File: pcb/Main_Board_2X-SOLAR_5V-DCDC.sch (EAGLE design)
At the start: 67 parts, among them CN5 USBA_FEMALE, M3AB FDMC8030, M4 SI7611DN, M5 FDMC8327L, T2 MMUN2133LT1G, U1 LTC4015EUHFPBFQFN-38_UHF-M, U3 TPS61090RSAR, X1 6V_PV

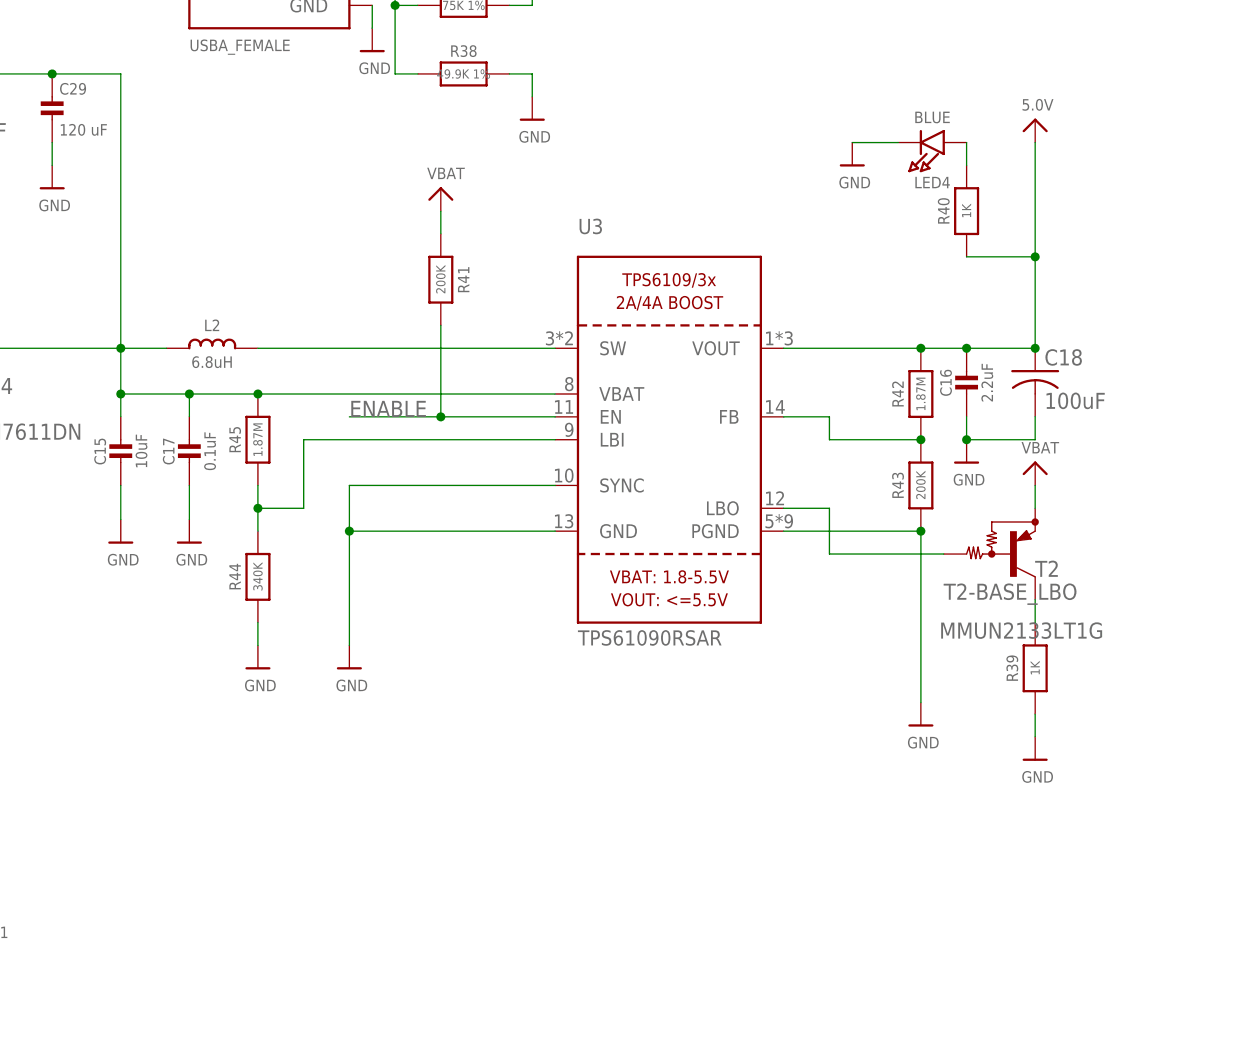
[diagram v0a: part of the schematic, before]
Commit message: PCB ready to print, reviewing
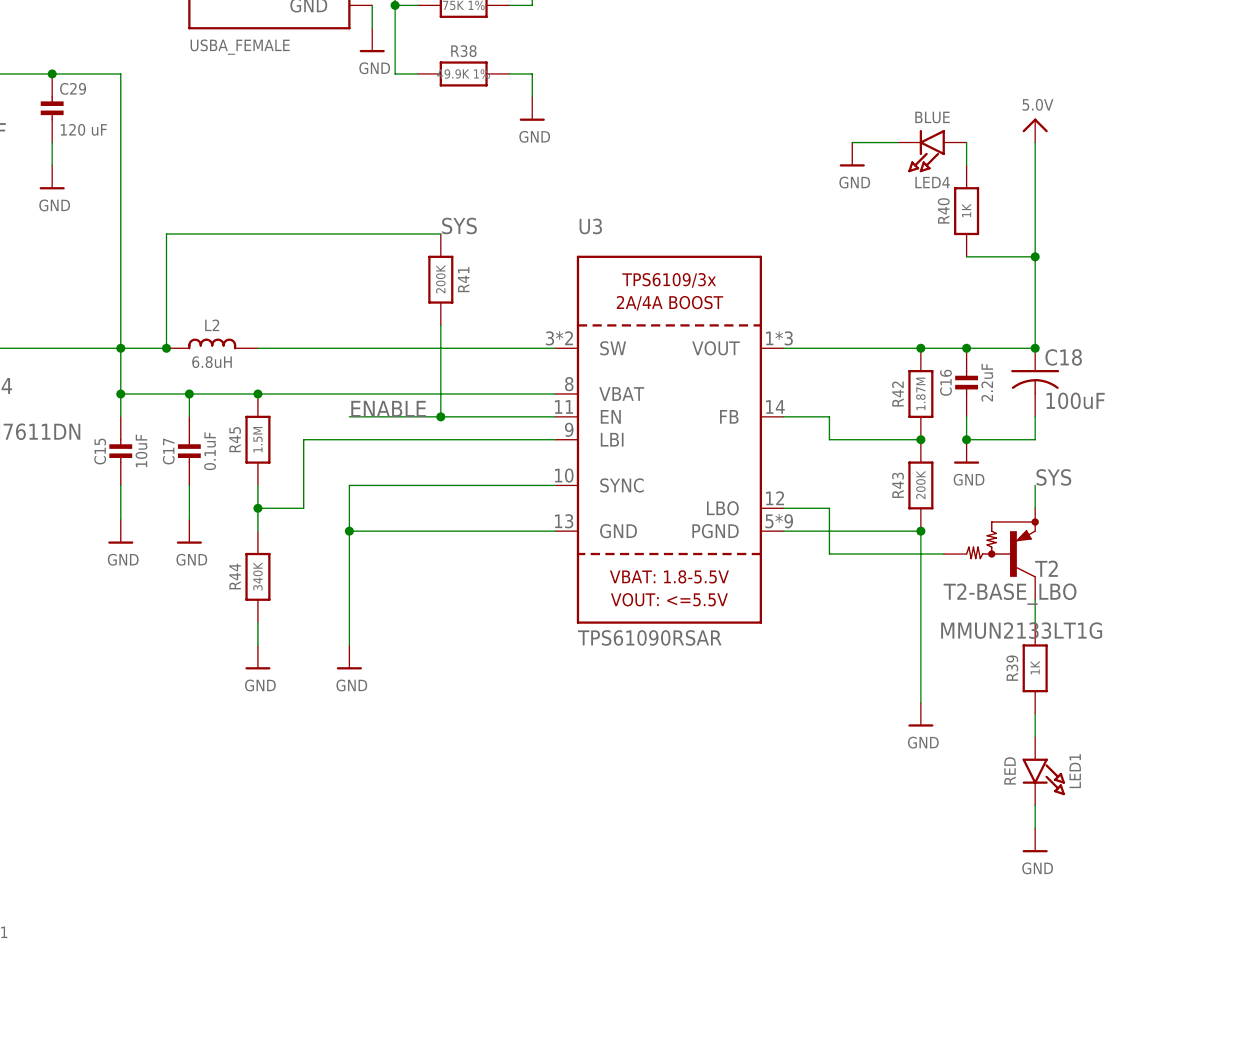
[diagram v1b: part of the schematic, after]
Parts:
- added LED1: RED, microbuilder:LED0805_NOOUTLINE
- R45: value 1.87M -> 1.5M
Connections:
- removed net VBAT: JP10.3, R41.1, T2.E
- new net N$1: LED1.A, R39.1
- net GND: now also LED1.C; no longer R39.1
- net SYS: now also JP10.3, R41.1, T2.E

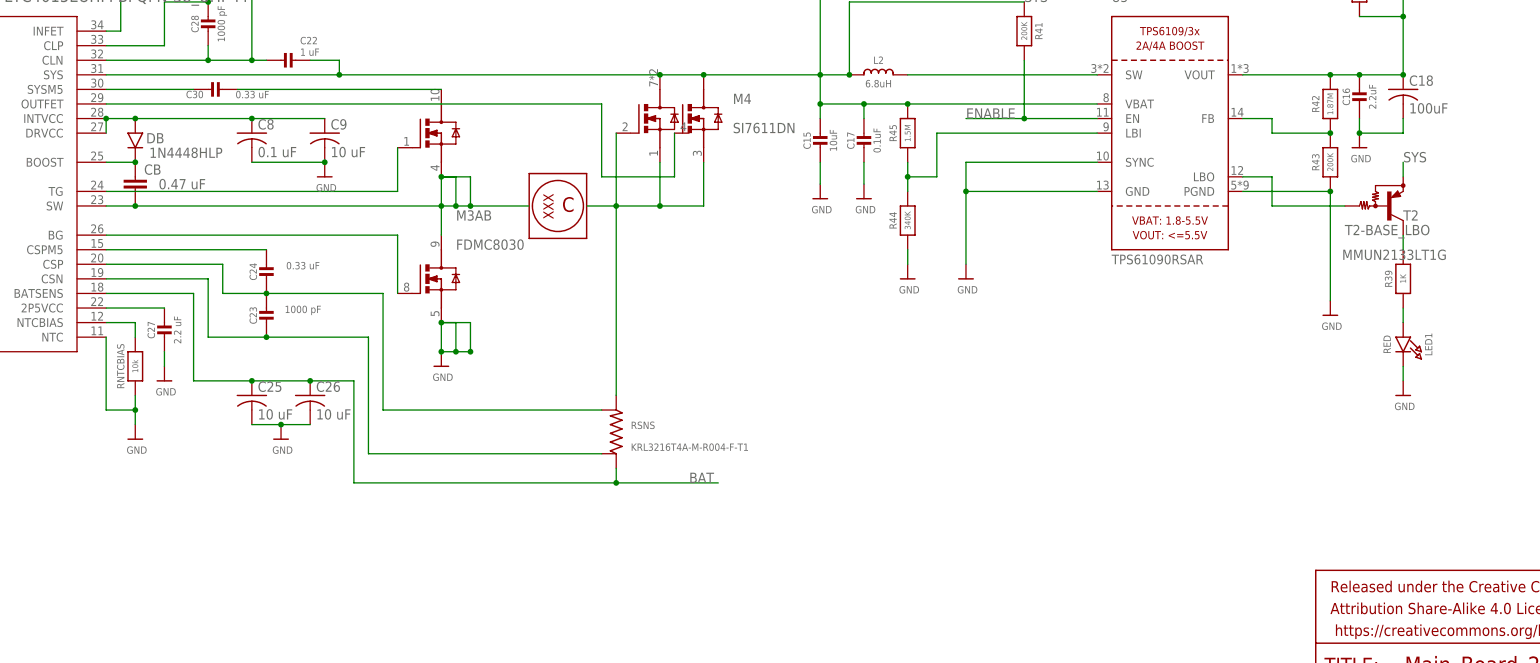
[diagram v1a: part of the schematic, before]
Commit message: OSH V1 print board and schematic update
Finalized routings for signal and power. Updated silkscreen text for clarity during assembly.
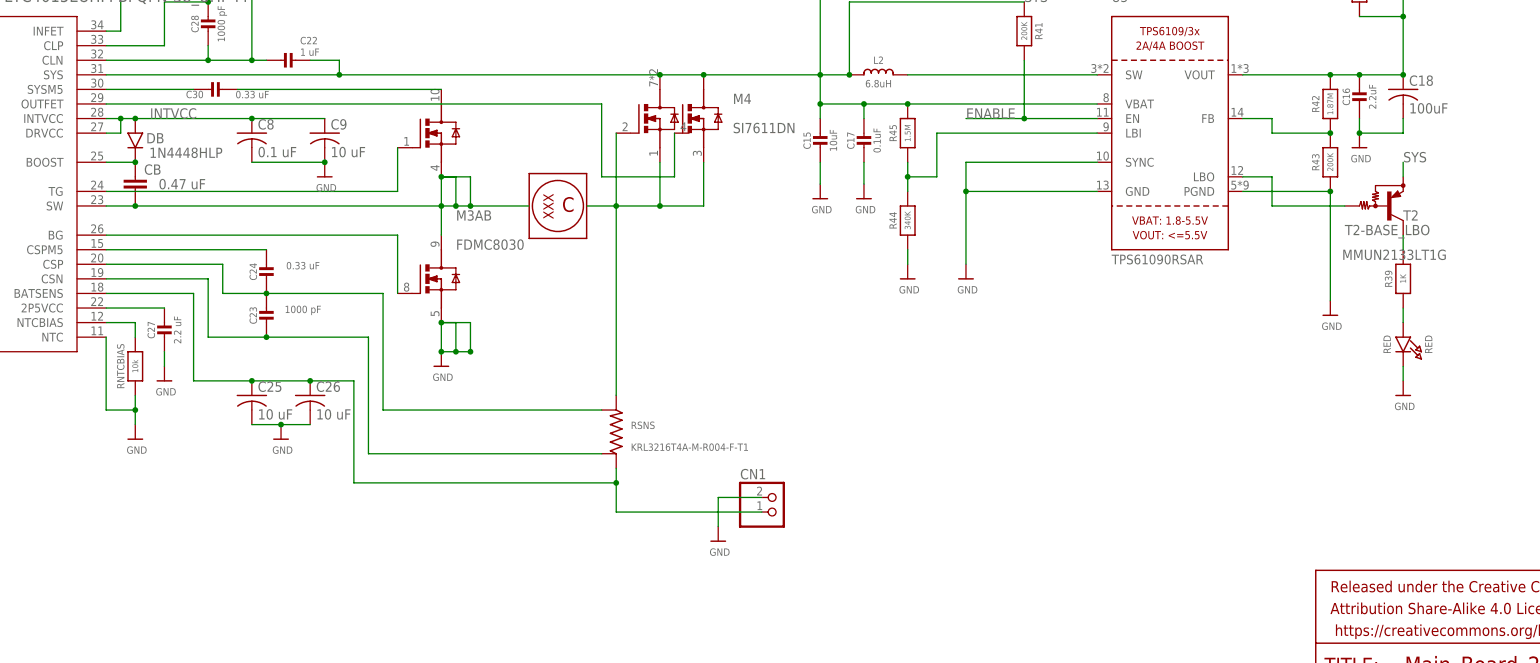
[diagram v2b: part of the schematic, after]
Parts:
- added CN1: (no value), adafruit:JST_2PIN-THM
- renumbered LED1 to RED
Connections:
- net BAT: now also CN1.2
- net GND: now also CN1.1
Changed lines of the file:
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@@
 <grid distance="0.1" unitdist="inch" unit="inch" style="lines" multiple="1" display="no" altdistance="0.01" altunitdist="inch" altunit="inch"/>
 <layers>
-<layer number="1" name="Top" color="4" fill="1" visible="yes" active="no"/>
-<layer number="16" name="Bottom" color="1" fill="1" visible="yes" active="no"/>
-<layer number="17" name="Pads" color="2" fill="1" visible="yes" active="no"/>
-<layer number="18" name="Vias" color="2" fill="1" visible="yes" active="no"/>
-<layer number="19" name="Unrouted" color="61" fill="1" visible="yes" active="no"/>
-<layer number="20" name="Dimension" color="15" fill="1" visible="yes" active="no"/>
-<layer number="21" name="tPlace" color="7" fill="1" visible="yes" active="no"/>
-<layer number="22" name="bPlace" color="7" fill="1" visible="yes" active="no"/>
-<layer number="23" name="tOrigins" color="15" fill="1" visible="yes" active="no"/>
-<layer number="24" name="bOrigins" color="15" fill="1" visible="yes" active="no"/>
-<layer number="25" name="tNames" color="7" fill="1" visible="yes" active="no"/>
-<layer number="26" name="bNames" color="7" fill="1" visible="yes" active="no"/>
-<layer number="27" name="tValues" color="7" fill="1" visible="yes" active="no"/>
-<layer number="28" name="bValues" color="7" fill="1" visible="yes" active="no"/>
+<layer number="1" name="Top" color="4" fill="1" visible="no" active="no"/>
+<layer number="16" name="Bottom" color="1" fill="1" visible="no" active="no"/>
+<layer number="17" name="Pads" color="2" fill="1" visible="no" active="no"/>
+<layer number="18" name="Vias" color="2" fill="1" visible="no" active="no"/>
+<layer number="19" name="Unrouted" color="61" fill="1" visible="no" active="no"/>
+<layer number="20" name="Dimension" color="15" fill="1" visible="no" active="no"/>
+<layer number="21" name="tPlace" color="7" fill="1" visible="no" active="no"/>
+<layer number="22" name="bPlace" color="7" fill="1" visible="no" active="no"/>
+<layer number="23" name="tOrigins" color="15" fill="1" visible="no" active="no"/>
+<layer number="24" name="bOrigins" color="15" fill="1" visible="no" active="no"/>
+<layer number="25" name="tNames" color="7" fill="1" visible="no" active="no"/>
+<layer number="26" name="bNames" color="7" fill="1" visible="no" active="no"/>
+<layer number="27" name="tValues" color="7" fill="1" visible="no" active="no"/>
+<layer number="28" name="bValues" color="7" fill="1" visible="no" active="no"/>
 <layer number="29" name="tStop" color="7" fill="3" visible="no" active="no"/>
 <layer number="30" name="bStop" color="7" fill="6" visible="no" active="no"/>
@@
 <layer number="35" name="tGlue" color="7" fill="4" visible="no" active="no"/>
 <layer number="36" name="bGlue" color="7" fill="5" visible="no" active="no"/>
-<layer number="37" name="tTest" color="7" fill="1" visible="yes" active="no"/>
-<layer number="38" name="bTest" color="7" fill="1" visible="yes" active="no"/>
+<layer number="37" name="tTest" color="7" fill="1" visible="no" active="no"/>
+<layer number="38" name="bTest" color="7" fill="1" visible="no" active="no"/>
 <layer number="39" name="tKeepout" color="4" fill="11" visible="no" active="no"/>
 <layer number="40" name="bKeepout" color="1" fill="11" visible="no" active="no"/>
@@
 <layer number="44" name="Drills" color="7" fill="1" visible="no" active="no"/>
 <layer number="45" name="Holes" color="7" fill="1" visible="no" active="no"/>
-<layer number="46" name="Milling" color="3" fill="1" visible="yes" active="no"/>
-<layer number="47" name="Measures" color="7" fill="1" visible="yes" active="no"/>
-<layer number="48" name="Document" color="7" fill="1" visible="yes" active="no"/>
-<layer number="49" name="Reference" color="7" fill="1" visible="yes" active="no"/>
-<layer number="50" name="dxf" color="7" fill="1" visible="yes" active="no"/>
-<layer number="51" name="tDocu" color="7" fill="1" visible="yes" active="no"/>
-<layer number="52" name="bDocu" color="7" fill="1" visible="yes" active="no"/>
-<layer number="53" name="tGND_GNDA" color="7" fill="9" visible="yes" active="no"/>
-<layer number="54" name="bGND_GNDA" color="1" fill="9" visible="yes" active="no"/>
-<layer number="56" name="wert" color="7" fill="1" visible="yes" active="no"/>
-<layer number="57" name="tCAD" color="7" fill="1" visible="yes" active="no"/>
-<layer number="59" name="tCarbon" color="7" fill="1" visible="yes" active="no"/>
-<layer number="60" name="bCarbon" color="7" fill="1" visible="yes" active="no"/>
+<layer number="46" name="Milling" color="3" fill="1" visible="no" active="no"/>
+<layer number="47" name="Measures" color="7" fill="1" visible="no" active="no"/>
+<layer number="48" name="Document" color="7" fill="1" visible="no" active="no"/>
+<layer number="49" name="Reference" color="7" fill="1" visible="no" active="no"/>
+<layer number="50" name="dxf" color="7" fill="1" visible="no" active="no"/>
+<layer number="51" name="tDocu" color="7" fill="1" visible="no" active="no"/>
+<layer number="52" name="bDocu" color="7" fill="1" visible="no" active="no"/>
+<layer number="53" name="tGND_GNDA" color="7" fill="9" visible="no" active="no"/>
+<layer number="54" name="bGND_GNDA" color="1" fill="9" visible="no" active="no"/>
+<layer number="56" name="wert" color="7" fill="1" visible="no" active="no"/>
+<layer number="57" name="tCAD" color="7" fill="1" visible="no" active="no"/>
+<layer number="59" name="tCarbon" color="7" fill="1" visible="no" active="no"/>
+<layer number="60" name="bCarbon" color="7" fill="1" visible="no" active="no"/>
 <layer number="90" name="Modules" color="5" fill="1" visible="yes" active="yes"/>
 <layer number="91" name="Nets" color="2" fill="1" visible="yes" active="yes"/>
@@
 <part name="C30" library="microbuilder" deviceset="CAP_CERAMIC" device="0805-NOOUTLINE" value="0.33 uF"/>
 <part name="JP1" library="pinhead" library_urn="urn:adsk.eagle:library:325" deviceset="PINHD-1X5" device=""/>
-<part name="LED1" library="microbuilder" deviceset="LED" device="0805_NOOUTLINE" value="RED"/>
+<part name="RED" library="microbuilder" deviceset="LED" device="0805_NOOUTLINE" value="RED"/>
+<part name="CN1" library="adafruit" library_urn="urn:adsk.eagle:library:420" deviceset="JST_2PIN" device="-THM"/>
+<part name="U$12" library="microbuilder" deviceset="GND" device=""/>
 </parts>
 <sheets>
@@
 </instance>
 <instance part="JP1" gate="A" x="7.62" y="93.98" rot="R180"/>
-<instance part="LED1" gate="G$1" x="345.44" y="73.66" rot="R270"/>
+<instance part="RED" gate="G$1" x="345.44" y="73.66" rot="R270"/>
+<instance part="CN1" gate="G$1" x="236.22" y="45.72"/>
+<instance part="U$12" gate="G$1" x="226.06" y="40.64"/>
 </instances>
 <busses>
@@
 <segment>
 <pinref part="U$70" gate="G$1" pin="GND"/>
-<pinref part="LED1" gate="G$1" pin="C"/>
+<pinref part="RED" gate="G$1" pin="C"/>
 <wire x1="345.44" y1="71.12" x2="345.44" y2="68.58" width="0.1524" layer="91"/>
+</segment>
+<segment>
+<pinref part="U$12" gate="G$1" pin="GND"/>
+<wire x1="226.06" y1="43.18" x2="226.06" y2="48.26" width="0.1524" layer="91"/>
+<pinref part="CN1" gate="G$1" pin="1"/>
+<wire x1="226.06" y1="48.26" x2="233.68" y2="48.26" width="0.1524" layer="91"/>
 </segment>
 </net>
@@
 <pinref part="U1" gate="A" pin="DRVCC"/>
 <pinref part="U1" gate="A" pin="INTVCC"/>
-<wire x1="119.38" y1="111.76" x2="119.38" y2="114.3" width="0.1524" layer="91"/>
-<junction x="119.38" y="114.3"/>
 <pinref part="C9" gate="G$1" pin="1"/>
-<wire x1="124.46" y1="114.3" x2="144.78" y2="114.3" width="0.1524" layer="91"/>
-<wire x1="157.48" y1="114.3" x2="144.78" y2="114.3" width="0.1524" layer="91"/>
 <junction x="144.78" y="114.3"/>
 <pinref part="DB" gate="G$1" pin="P$2"/>
 <junction x="124.46" y="114.3"/>
-<wire x1="119.38" y1="114.3" x2="124.46" y2="114.3" width="0.1524" layer="91"/>
+<wire x1="119.38" y1="114.3" x2="121.92" y2="114.3" width="0.1524" layer="91"/>
+<wire x1="121.92" y1="114.3" x2="124.46" y2="114.3" width="0.1524" layer="91"/>
+<junction x="121.92" y="114.3"/>
+<wire x1="121.92" y1="111.76" x2="119.38" y2="111.76" width="0.1524" layer="91"/>
+<wire x1="124.46" y1="114.3" x2="144.78" y2="114.3" width="0.1524" layer="91"/>
+<wire x1="144.78" y1="114.3" x2="157.48" y2="114.3" width="0.1524" layer="91"/>
+<wire x1="121.92" y1="114.3" x2="121.92" y2="111.76" width="0.1524" layer="91"/>
+<label x="127" y="114.3" size="1.778" layer="95"/>
 </segment>
 <segment>
@@
 <junction x="154.94" y="68.58"/>
 <wire x1="162.56" y1="50.8" x2="208.28" y2="50.8" width="0.1524" layer="91"/>
-<label x="220.98" y="50.8" size="1.778" layer="95"/>
 <pinref part="RSNS" gate="R1" pin="2"/>
-<wire x1="208.28" y1="50.8" x2="226.06" y2="50.8" width="0.1524" layer="91"/>
 <wire x1="208.28" y1="53.34" x2="208.28" y2="50.8" width="0.1524" layer="91"/>
+<pinref part="CN1" gate="G$1" pin="2"/>
+<wire x1="233.68" y1="45.72" x2="208.28" y2="45.72" width="0.1524" layer="91"/>
+<wire x1="208.28" y1="45.72" x2="208.28" y2="50.8" width="0.1524" layer="91"/>
 <junction x="208.28" y="50.8"/>
 </segment>
@@
 <segment>
 <pinref part="R39" gate="G$1" pin="1"/>
-<pinref part="LED1" gate="G$1" pin="A"/>
+<pinref part="RED" gate="G$1" pin="A"/>
 <wire x1="345.44" y1="78.74" x2="345.44" y2="81.28" width="0.1524" layer="91"/>
 </segment>
@@
 </sheet>
 </sheets>
+<errors>
+</errors>
 </schematic>
 </drawing>
